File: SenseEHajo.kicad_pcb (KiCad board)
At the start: 2 copper layers, 141 x 56.9 mm, 75 parts, among them IC1 AP3012, IC2 MCP3221, IC3 SN74AUP1G08-Q1, J1 Conn_01x02_Male, J2 REED, J3 RTC ( DS3231), J4 Heizung, J5 Pumpe, J6 Conn_01x05, J7 L, J8 N, J9 Prog, Q1 BSS138, SW1 Reset, SW2 SW1 ( Boot ), SW3 SW2, SW4 SW3, T1 QJ8025, T2 QJ8025, U1 ESP32-WROOM-32, U2 MCP6001-OT, U3 MOC3043M, U4 MOC3043M, U5 TCA9544A, U6 LM1117-3.3

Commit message: CleanUp
Small Cleanup on the PCB
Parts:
- added C18: 10uF, Capacitor_SMD:C_0805_2012Metric_Pad1.15x1.40mm_HandSolder, F.Cu at (154.1, 25.0)
- added C19: 100nF, Capacitor_SMD:C_0805_2012Metric_Pad1.15x1.40mm_HandSolder, F.Cu at (154.1, 26.9)
- moved C4 2.55 mm to (152.7, 28.9), turned to 180 degrees
- moved J6 0.05 mm to (133.2, 68.6)
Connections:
- J3 pad 4: (no net) -> Net-(J3-Pad4)
- LED3 pad 1: (no net) -> Net-(LED3-Pad1)
- U1 pad 10: (no net) -> IO25
- U1 pad 13: (no net) -> IO14
- U1 pad 14: (no net) -> IO12
- U1 pad 16: (no net) -> IO13
- U1 pad 17: (no net) -> Net-(U1-Pad17)
- U1 pad 18: (no net) -> Net-(U1-Pad18)
- U1 pad 19: (no net) -> Net-(U1-Pad19)
- U1 pad 20: (no net) -> Net-(U1-Pad20)
- U1 pad 21: (no net) -> Net-(U1-Pad21)
- U1 pad 22: (no net) -> Net-(U1-Pad22)
- U1 pad 23: (no net) -> IO15
- U1 pad 24: (no net) -> IO2
- U1 pad 30: (no net) -> IO18
- U1 pad 31: (no net) -> IO19
- U1 pad 32: (no net) -> Net-(U1-Pad32)
- U1 pad 37: (no net) -> IO23
- U1 pad 4: (no net) -> SVP
- U1 pad 5: (no net) -> SVN
- U1 pad 6: (no net) -> IO34
- U1 pad 7: (no net) -> IO35
- U3 pad 3: (no net) -> Net-(U3-Pad3)
- U3 pad 5: (no net) -> Net-(U3-Pad5)
- U4 pad 3: (no net) -> Net-(U4-Pad3)
- U4 pad 5: (no net) -> Net-(U4-Pad5)
- U5 pad 11: (no net) -> Net-(U5-Pad11)
- U5 pad 14: (no net) -> Net-(U5-Pad14)
- U5 pad 15: (no net) -> Net-(U5-Pad15)
- U5 pad 16: (no net) -> Net-(U5-Pad16)
- U5 pad 4: (no net) -> Net-(U5-Pad4)
- U5 pad 7: (no net) -> Net-(U5-Pad7)
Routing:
- net GND: track 291.9 -> 283.4 mm, vias 2 -> 78
- net Net-(C1-Pad1): track 49.3 -> 53.8 mm
- net +3V3: track 260.5 -> 264.0 mm
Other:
- board text added: "3V3"
- board text added: "5V"
- board text added: "GND"
- board text added: "Heater"
- board text added: "MCU_RX"
- board text added: "MCU_TX"
- board text added: "Pump"
- board text added: "Schematic + Routing by CalM"
- board text removed: "ACDC1"
- board text removed: "C6"
- board text removed: "C7"
- board text removed: "LED2"
- board text removed: "LED3"
- board text removed: "Schematic and Routing by CalM"

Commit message: Added Netfrequency Detection
This will detect the Netfrequency on IO25 of the ESP32. This is usefull to determine the amount of water pumped to the cup
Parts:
- added IC4: K814P, Package_DIP:DIP-4_W7.62mm, F.Cu at (44.1, 66.0)
- added R5: 10k, Resistor_SMD:R_0805_2012Metric_Pad1.15x1.40mm_HandSolder, F.Cu at (76.1, 64.5)
- added R6: 100k, Resistor_THT:R_Axial_DIN0207_L6.3mm_D2.5mm_P7.62mm_Horizontal, F.Cu at (33.5, 63.0)
- added R7: 100k, Resistor_THT:R_Axial_DIN0207_L6.3mm_D2.5mm_P7.62mm_Horizontal, F.Cu at (24.9, 54.8)
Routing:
- net IO25: track 0.00 -> 140.0 mm, vias 0 -> 7
- net N_230V: track 20.8 -> 48.8 mm
- net L_230V: track 141.2 -> 159.4 mm
- net GND: track 283.4 -> 290.6 mm
- net Net-(IC4-Pad2): track 0.00 -> 5.70 mm
- net +3V3: track 264.0 -> 268.8 mm
- net Net-(R6-Pad1): track 0.00 -> 4.33 mm
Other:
- outline, holes or cut-outs redrawn

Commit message: Small modifications
The AC/DC supply is operating on the edge of it's limits now
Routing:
- net GND: track 290.6 -> 264.2 mm
- net +5V: track 317.7 -> 313.3 mm, vias 5 -> 7
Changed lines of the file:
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@@
     (thickness 1.6)
     (drawings 592)
-    (tracks 1166)
+    (tracks 1169)
     (zones 0)
     (modules 81)
@@
   (segment (start 122.27921 61.74379) (end 119.32682 61.74379) (width 0.25) (layer F.Cu) (net 2))
   (segment (start 124.587 59.436) (end 122.27921 61.74379) (width 0.25) (layer F.Cu) (net 2))
-  (segment (start 60.724644 48.744869) (end 72.413131 48.744869) (width 0.25) (layer F.Cu) (net 2))
-  (segment (start 59.574645 47.59487) (end 60.724644 48.744869) (width 0.25) (layer F.Cu) (net 2))
-  (segment (start 72.413131 48.744869) (end 74.60679 46.55121) (width 0.25) (layer F.Cu) (net 2))
   (segment (start 105.5116 46.8884) (end 105.156 47.244) (width 0.25) (layer F.Cu) (net 2))
   (segment (start 108.368731 52.750429) (end 103.550429 52.750429) (width 0.25) (layer F.Cu) (net 2))
@@
   (segment (start 95.5294 46.988402) (end 95.504 45.4914) (width 0.25) (layer F.Cu) (net 2))
   (segment (start 95.504 45.4914) (end 95.5294 44.9592) (width 0.25) (layer F.Cu) (net 2))
-  (segment (start 83.09039 46.55121) (end 84.1502 45.4914) (width 0.25) (layer F.Cu) (net 2))
-  (segment (start 83.09039 46.55121) (end 74.60679 46.55121) (width 0.25) (layer F.Cu) (net 2))
   (segment (start 140.875001 67.404999) (end 142.533001 65.746999) (width 0.25) (layer B.Cu) (net 2))
   (segment (start 139.528801 67.404999) (end 140.875001 67.404999) (width 0.25) (layer B.Cu) (net 2))
@@
   (via (at 144.0434 42.9006) (size 0.8) (drill 0.4) (layers F.Cu B.Cu) (net 2))
   (via (at 143.7894 39.0906) (size 0.8) (drill 0.4) (layers F.Cu B.Cu) (net 2))
-  (via (at 143.8656 35.687) (size 0.8) (drill 0.4) (layers F.Cu B.Cu) (net 2))
+  (via (at 143.8656 35.9664) (size 0.8) (drill 0.4) (layers F.Cu B.Cu) (net 2))
   (segment (start 148.971 38.989) (end 148.971 38.989) (width 1) (layer F.Cu) (net 2))
   (via (at 148.971 38.989) (size 0.8) (drill 0.4) (layers F.Cu B.Cu) (net 2))
@@
   (segment (start 73.047862 69.25599) (end 73.61901 69.827138) (width 1.5) (layer B.Cu) (net 8))
   (segment (start 70.62759 69.25599) (end 73.047862 69.25599) (width 1.5) (layer B.Cu) (net 8))
-  (segment (start 131.4238 68.58) (end 130.485799 69.518001) (width 1) (layer B.Cu) (net 8))
   (segment (start 133.2738 68.58) (end 131.4238 68.58) (width 1) (layer B.Cu) (net 8))
-  (segment (start 125.857 65.5066) (end 125.857 59.436) (width 1) (layer B.Cu) (net 8))
   (via (at 113.1062 56.4896) (size 0.8) (drill 0.4) (layers F.Cu B.Cu) (net 8))
   (segment (start 113.1062 54.0692) (end 114.808 52.3674) (width 1) (layer F.Cu) (net 8))
@@
   (segment (start 119.509402 45.087402) (end 108.1532 45.0596) (width 1) (layer B.Cu) (net 8))
   (segment (start 128.982999 69.518001) (end 128.238999 69.518001) (width 1) (layer B.Cu) (net 8))
-  (segment (start 130.485799 69.518001) (end 128.982999 69.518001) (width 1) (layer B.Cu) (net 8))
   (segment (start 114.200199 69.518001) (end 113.6142 70.104) (width 1) (layer B.Cu) (net 8))
   (segment (start 113.6142 70.104) (end 113.6142 75.9206) (width 1) (layer B.Cu) (net 8))
-  (segment (start 125.8824 60.168506) (end 125.8824 69.5706) (width 1) (layer B.Cu) (net 8))
-  (segment (start 125.857 60.143106) (end 125.8824 60.168506) (width 1) (layer B.Cu) (net 8))
-  (segment (start 128.982999 69.518001) (end 125.8824 69.5706) (width 1) (layer B.Cu) (net 8))
-  (segment (start 125.857 59.436) (end 125.857 60.143106) (width 1) (layer B.Cu) (net 8))
-  (segment (start 125.8824 69.5706) (end 114.200199 69.518001) (width 1) (layer B.Cu) (net 8))
+  (segment (start 125.8824 60.117706) (end 125.8824 69.5198) (width 1) (layer B.Cu) (net 8))
   (segment (start 124.333 35.151198) (end 124.3584 35.125798) (width 1) (layer B.Cu) (net 8))
   (segment (start 124.333 36.703) (end 124.333 35.151198) (width 1) (layer B.Cu) (net 8))
@@
   (segment (start 104.14 69.215) (end 104.14 71.0184) (width 0.25) (layer B.Cu) (net 8))
   (segment (start 103.8606 68.9356) (end 104.14 69.215) (width 0.25) (layer B.Cu) (net 8))
-  (segment (start 61.5442 58.220894) (end 74.705494 45.0596) (width 1) (layer B.Cu) (net 8))
+  (segment (start 61.5442 58.220894) (end 65.165747 54.599347) (width 1) (layer B.Cu) (net 8))
   (segment (start 61.5442 58.928) (end 61.5442 58.220894) (width 1) (layer B.Cu) (net 8))
   (segment (start 108.1532 45.0596) (end 77.6478 45.0596) (width 1) (layer B.Cu) (net 8))
   (segment (start 74.705494 45.0596) (end 77.6478 45.0596) (width 1) (layer B.Cu) (net 8))
+  (via (at 65.165747 54.599347) (size 0.8) (drill 0.4) (layers F.Cu B.Cu) (net 8))
+  (segment (start 72.836547 46.928547) (end 74.705494 45.0596) (width 1) (layer B.Cu) (net 8))
+  (via (at 72.836547 46.928547) (size 0.8) (drill 0.4) (layers F.Cu B.Cu) (net 8))
+  (segment (start 65.565746 54.199348) (end 72.836547 46.928547) (width 1) (layer F.Cu) (net 8))
+  (segment (start 65.165747 54.599347) (end 65.565746 54.199348) (width 1) (layer F.Cu) (net 8))
+  (segment (start 114.200199 69.518001) (end 123.467601 69.518001) (width 1) (layer B.Cu) (net 8))
+  (segment (start 130.485799 69.518001) (end 130.556 69.5198) (width 1) (layer B.Cu) (net 8))
+  (segment (start 123.4694 69.5198) (end 130.556 69.5198) (width 1) (layer B.Cu) (net 8))
+  (segment (start 123.467601 69.518001) (end 123.4694 69.5198) (width 1) (layer B.Cu) (net 8))
+  (segment (start 130.556 69.5198) (end 128.982999 69.518001) (width 1) (layer B.Cu) (net 8))
+  (segment (start 130.556 69.4478) (end 131.4238 68.58) (width 1) (layer B.Cu) (net 8))
+  (segment (start 130.556 69.5198) (end 130.556 69.4478) (width 1) (layer B.Cu) (net 8))
+  (segment (start 125.8824 59.5122) (end 125.8824 60.117706) (width 1) (layer B.Cu) (net 8))
+  (segment (start 125.857 59.4868) (end 125.8824 59.5122) (width 1) (layer B.Cu) (net 8))
+  (segment (start 125.857 59.436) (end 125.857 59.4868) (width 1) (layer B.Cu) (net 8))
   (segment (start 113.6122 70.4142) (end 113.4798 70.2818) (width 1) (layer F.Cu) (net 9))
   (segment (start 113.6122 72.4916) (end 113.6122 70.4142) (width 1) (layer F.Cu) (net 9))

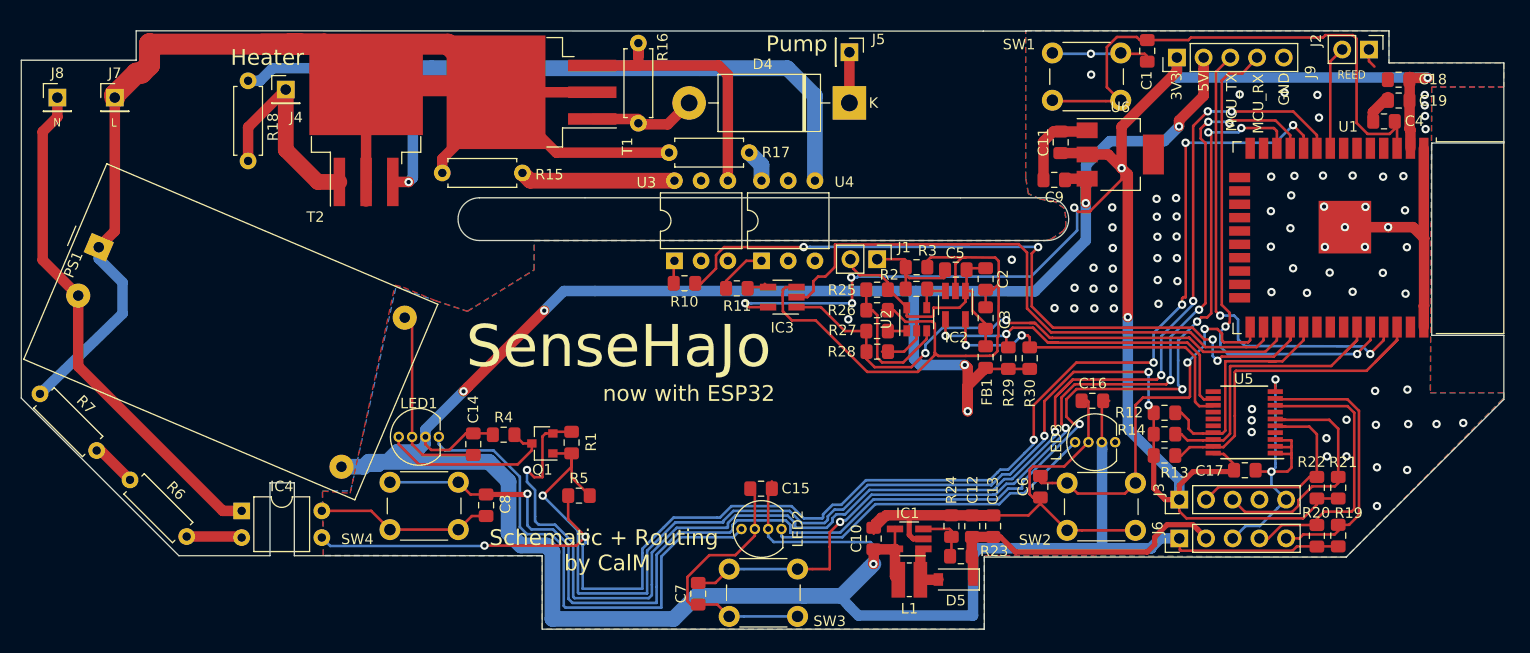
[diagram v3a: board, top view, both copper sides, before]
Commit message: Version3
Ordered Proto for Version 3
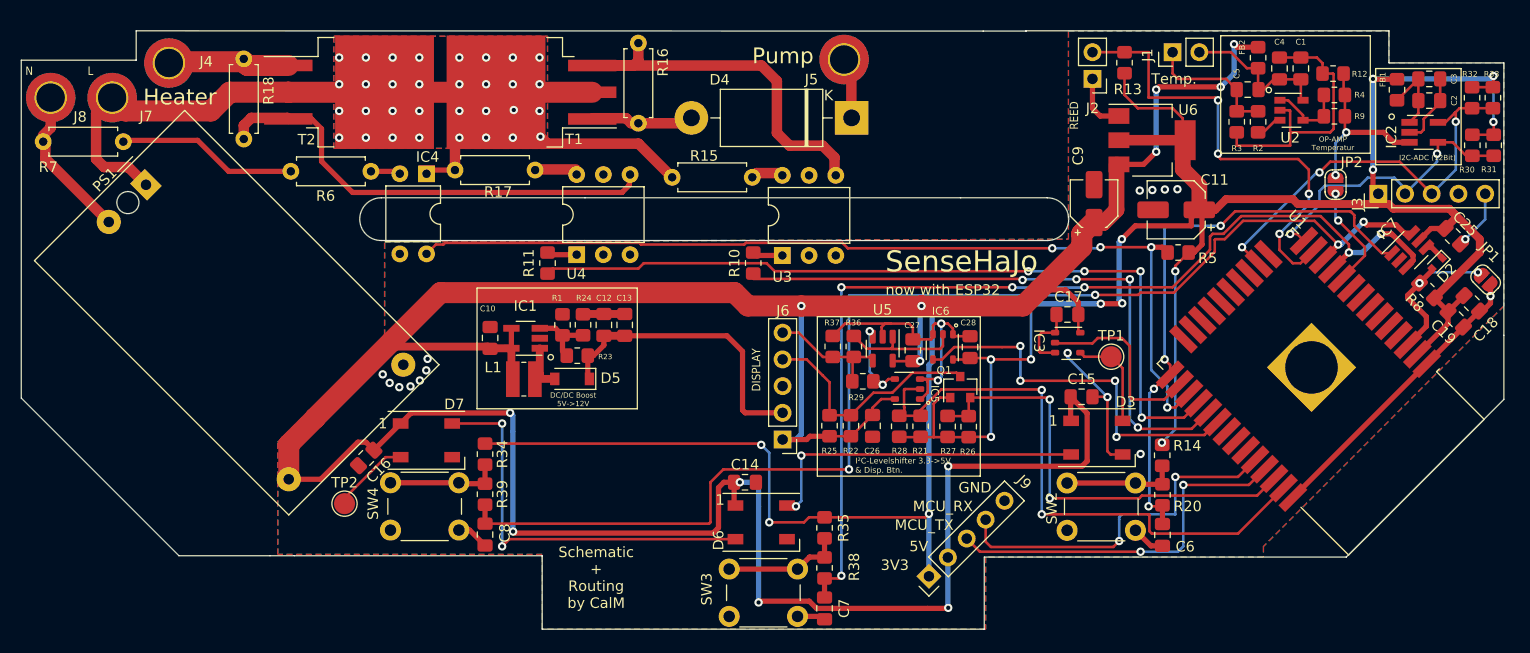
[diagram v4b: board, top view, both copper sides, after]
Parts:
- removed LED1, LED2, LED3: WS2812D, WS2812D:WS2812D_THT
- removed R19: 15k, Resistor_SMD:R_0805_2012Metric_Pad1.15x1.40mm_HandSolder
- removed SW1: Reset, Button_Switch_THT:SW_PUSH_6mm
- added C25: 100nF / 10V, Capacitor_SMD:C_0805_2012Metric_Pad1.18x1.45mm_HandSolder, F.Cu at (159.2, 39.8)
- added C26: 100nF / 10V, Capacitor_SMD:C_0805_2012Metric_Pad1.18x1.45mm_HandSolder, F.Cu at (104.1, 57.9)
- added C27: 100nF / 10V, Capacitor_SMD:C_0805_2012Metric_Pad1.18x1.45mm_HandSolder, F.Cu at (107.9, 50.7)
- added C28: 100nF / 10V, Capacitor_SMD:C_0805_2012Metric_Pad1.18x1.45mm_HandSolder, F.Cu at (113.3, 50.4)
- added D2: D_Schottky, Diode_SMD:D_SOD-523, F.Cu at (157.7, 42.4)
- added D3: WS2812B, LED_SMD:LED_WS2812B_PLCC4_5.0x5.0mm_P3.2mm, F.Cu at (125.4, 59.0)
- added D6: WS2812B, LED_SMD:LED_WS2812B_PLCC4_5.0x5.0mm_P3.2mm, F.Cu at (93.5, 67.1)
- added D7: WS2812B, LED_SMD:LED_WS2812B_PLCC4_5.0x5.0mm_P3.2mm, F.Cu at (61.6, 59.3)
- added FB2: Ferrite_Bead, Resistor_SMD:R_0805_2012Metric_Pad1.20x1.40mm_HandSolder, F.Cu at (140.7, 22.9)
- added IC5: 74LVC1G125, SC-74A_SOT753:SC-74A, F.Cu at (108.6, 55.3)
- added IC6: 74LVC1G125, SC-74A_SOT753:SC-74A, F.Cu at (111.7, 49.2)
- added IC7: 74LVC1G10, Package_TO_SOT_SMD:SOT-23-6_Handsoldering, F.Cu at (155.1, 41.2)
- added JP1: Jumper_2_Open, Jumper:SolderJumper-2_P1.3mm_Open_RoundedPad1.0x1.5mm, F.Cu at (162.4, 44.0)
- added JP2: Jumper_2_Open, Jumper:SolderJumper-2_P1.3mm_Open_RoundedPad1.0x1.5mm, F.Cu at (148.1, 34.9)
- added R31: 10k, Resistor_SMD:R_0805_2012Metric_Pad1.20x1.40mm_HandSolder, F.Cu at (163.1, 31.2)
- added R32: 10k, Resistor_SMD:R_0805_2012Metric_Pad1.20x1.40mm_HandSolder, F.Cu at (161.1, 26.7)
- added R33: 10k, Resistor_SMD:R_0805_2012Metric_Pad1.20x1.40mm_HandSolder, F.Cu at (163.0, 26.7)
- added R34: 10k, Resistor_SMD:R_0805_2012Metric_Pad1.20x1.40mm_HandSolder, F.Cu at (67.2, 60.6)
- added R35: 10k, Resistor_SMD:R_0805_2012Metric_Pad1.20x1.40mm_HandSolder, F.Cu at (99.5, 67.6)
- added R36: 10k, Resistor_SMD:R_0805_2012Metric_Pad1.20x1.40mm_HandSolder, F.Cu at (102.3, 50.3)
- added R37: 1k, Resistor_SMD:R_0805_2012Metric_Pad1.20x1.40mm_HandSolder, F.Cu at (100.3, 50.3)
- added R38: 1k, Resistor_SMD:R_0805_2012Metric_Pad1.20x1.40mm_HandSolder, F.Cu at (99.5, 71.4)
- added R39: 1k, Resistor_SMD:R_0805_2012Metric_Pad1.20x1.40mm_HandSolder, F.Cu at (67.2, 64.4)
- added R8: 10k, Resistor_SMD:R_0805_2012Metric_Pad1.20x1.40mm_HandSolder, F.Cu at (156.8, 45.0)
- added R9: 10k, Resistor_SMD:R_0805_2012Metric_Pad1.20x1.40mm_HandSolder, F.Cu at (148.0, 28.4)
- added REF**: MountingHole_2.1mm, MountingHole:MountingHole_2.1mm, F.Cu at (33.2, 36.7)
- added TP1: TestPoint, TestPoint:TestPoint_Pad_D2.0mm, F.Cu at (126.7, 51.3)
- added TP2: TestPoint, TestPoint:TestPoint_Pad_D2.0mm, F.Cu at (53.8, 65.3)
- C1: value 100nF / 25V -> 1uF / 10V; footprint Capacitor_SMD:C_0805_2012Metric_Pad1.15x1.40mm_HandSolder -> Capacitor_SMD:C_0805_2012Metric_Pad1.18x1.45mm_HandSolder
- C10, C12, C13, C3: footprint Capacitor_SMD:C_0805_2012Metric_Pad1.15x1.40mm_HandSolder -> Capacitor_SMD:C_0805_2012Metric_Pad1.18x1.45mm_HandSolder
- C11: value 100uF -> 47uF/10V; footprint Capacitor_SMD:C_0805_2012Metric_Pad1.15x1.40mm_HandSolder -> Capacitor_SMD:CP_Elec_5x5.3
- C14, C15, C16, C17, C19, C5, C7, C8: value 100nF -> 100nF / 10V; footprint Capacitor_SMD:C_0805_2012Metric_Pad1.15x1.40mm_HandSolder -> Capacitor_SMD:C_0805_2012Metric_Pad1.18x1.45mm_HandSolder
- C18: value 10uF -> 10uF / 10V; footprint Capacitor_SMD:C_0805_2012Metric_Pad1.15x1.40mm_HandSolder -> Capacitor_SMD:C_0805_2012Metric_Pad1.18x1.45mm_HandSolder
- C2: value 100nf / 10V -> 100nF / 10V; footprint Capacitor_SMD:C_0805_2012Metric_Pad1.15x1.40mm_HandSolder -> Capacitor_SMD:C_0805_2012Metric_Pad1.18x1.45mm_HandSolder
- C4: value 10uF / 25V -> 100nF / 10V; footprint Capacitor_SMD:C_0805_2012Metric_Pad1.15x1.40mm_HandSolder -> Capacitor_SMD:C_0805_2012Metric_Pad1.18x1.45mm_HandSolder
- C6: value 100nF / 25V -> 100nF / 10V; footprint Capacitor_SMD:C_0805_2012Metric_Pad1.15x1.40mm_HandSolder -> Capacitor_SMD:C_0805_2012Metric_Pad1.18x1.45mm_HandSolder
- C9: value 10uF -> 10uF/10V; footprint Capacitor_SMD:C_0805_2012Metric_Pad1.15x1.40mm_HandSolder -> Capacitor_SMD:CP_Elec_4x4.5
- FB1: footprint Capacitor_SMD:C_0805_2012Metric_Pad1.15x1.40mm_HandSolder -> Resistor_SMD:R_0805_2012Metric_Pad1.20x1.40mm_HandSolder
- IC3: value SN74AUP1G08-Q1 -> 74LVC1G125; footprint Package_TO_SOT_SMD:SOT-23-5_HandSoldering -> SC-74A_SOT753:SC-74A
- J4: value Heizung -> Heizung L; footprint Connector_PinHeader_2.54mm:PinHeader_1x01_P2.54mm_Vertical -> MountingHole:MountingHole_2.7mm_M2.5_DIN965_Pad_TopBottom
- J5: value Pumpe -> Pumpe L; footprint Connector_PinHeader_2.54mm:PinHeader_1x01_P2.54mm_Vertical -> MountingHole:MountingHole_2.7mm_M2.5_DIN965_Pad_TopBottom
- J7, J8: footprint Connector_PinHeader_2.54mm:PinHeader_1x01_P2.54mm_Vertical -> MountingHole:MountingHole_2.7mm_M2.5_DIN965_Pad_TopBottom
- R1, R10, R11, R2, R3, R5: footprint Resistor_SMD:R_0805_2012Metric_Pad1.15x1.40mm_HandSolder -> Resistor_SMD:R_0805_2012Metric_Pad1.20x1.40mm_HandSolder
- R12, R24: value 4k7 -> 10k; footprint Resistor_SMD:R_0805_2012Metric_Pad1.15x1.40mm_HandSolder -> Resistor_SMD:R_0805_2012Metric_Pad1.20x1.40mm_HandSolder
- R13, R14, R21, R22, R30: value 2k2 -> 10k; footprint Resistor_SMD:R_0805_2012Metric_Pad1.15x1.40mm_HandSolder -> Resistor_SMD:R_0805_2012Metric_Pad1.20x1.40mm_HandSolder
- R20: value 15k -> 1k; footprint Resistor_SMD:R_0805_2012Metric_Pad1.15x1.40mm_HandSolder -> Resistor_SMD:R_0805_2012Metric_Pad1.20x1.40mm_HandSolder
- R23: value 39k -> 43.2k; footprint Resistor_SMD:R_0805_2012Metric_Pad1.15x1.40mm_HandSolder -> Resistor_SMD:R_0805_2012Metric_Pad1.20x1.40mm_HandSolder
- R25: value 1k -> 10k; footprint Resistor_SMD:R_0805_2012Metric_Pad1.15x1.40mm_HandSolder -> Resistor_SMD:R_0805_2012Metric_Pad1.20x1.40mm_HandSolder
- R26: value 3k9 -> 10k; footprint Resistor_SMD:R_0805_2012Metric_Pad1.15x1.40mm_HandSolder -> Resistor_SMD:R_0805_2012Metric_Pad1.20x1.40mm_HandSolder
- R27: value 1k8 -> 10k; footprint Resistor_SMD:R_0805_2012Metric_Pad1.15x1.40mm_HandSolder -> Resistor_SMD:R_0805_2012Metric_Pad1.20x1.40mm_HandSolder
- R28: value 3k3 -> 10k; footprint Resistor_SMD:R_0805_2012Metric_Pad1.15x1.40mm_HandSolder -> Resistor_SMD:R_0805_2012Metric_Pad1.20x1.40mm_HandSolder
- R29: value 2k2 -> 100R; footprint Resistor_SMD:R_0805_2012Metric_Pad1.15x1.40mm_HandSolder -> Resistor_SMD:R_0805_2012Metric_Pad1.20x1.40mm_HandSolder
- R4: value 10k -> 10k (DNP); footprint Resistor_SMD:R_0805_2012Metric_Pad1.15x1.40mm_HandSolder -> Resistor_SMD:R_0805_2012Metric_Pad1.20x1.40mm_HandSolder
- SW3: value SW2 -> MACHINE_SW2
- SW4: value SW3 -> MACHINE_SW3
- U1: footprint RF_Module:ESP32-WROOM-32 -> ESP32_Handsolder:ESP32-WROOM-32_HandSolder
- U5: value TCA9544A -> MCP6001-OT; footprint Package_SO:TSSOP-20_4.4x6.5mm_P0.65mm -> Package_TO_SOT_SMD:SOT-23-5
- U6: footprint Package_TO_SOT_SMD:SOT-223 -> Package_TO_SOT_SMD:SOT-223-3_TabPin2
- moved R4 85.3 mm to (148.0, 26.4), turned to 180 degrees
- moved C16 69.3 mm to (55.9, 60.9), turned to -135 degrees
- moved R5 61.5 mm to (133.1, 41.4)
- moved J9 54.7 mm to (109.4, 72.2), turned to 135 degrees
- moved C3 47.9 mm to (157.0, 24.9), turned to 0 degrees
- moved IC2 47.5 mm to (156.5, 30.0), turned to 0 degrees
- moved R30 46.7 mm to (161.1, 31.2)
- moved FB1 46.6 mm to (153.9, 25.9), turned to -90 degrees
- moved C2 45.5 mm to (157.0, 27.0), turned to 0 degrees
- moved R22 44.7 mm to (102.0, 57.9), turned to -90 degrees
- moved L1 41.3 mm to (70.9, 53.4)
- moved C10 41.2 mm to (67.7, 49.5)
- moved D5 41.2 mm to (75.5, 53.4)
- moved R23 41.2 mm to (76.0, 51.2)
- moved IC1 41.2 mm to (71.1, 49.6)
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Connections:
- C17 pad 2: +3V3 -> +5V
- C5 pad 1: Net-(C2-Pad1) -> Net-(C1-Pad1)
- C6 pad 2: Net-(C6-Pad2) -> SW1
- C7 pad 2: Net-(C7-Pad2) -> SW2
- C8 pad 2: Net-(C8-Pad2) -> SW3
- FB1 pad 1: +5V -> +3V3
- IC2 pad 4: SDA_ADC -> SDA_3V3
- IC2 pad 5: SCL_ADC -> SCL_3V3
- IC3 pad 1: ~OVERTEMP -> GND
- IC3 pad 2: Heizung -> WS2812_3V3
- IC3 pad 4: Net-(IC3-Pad4) -> Net-(D3-Pad4)
- IC3 pad 5: +3V3 -> +5V
- IC4 pad 1: N_230V -> L_230V
- IC4 pad 3: IO25 -> GND
- IC4 pad 4: GND -> MAINS_HALVEWAVES
- J1 pad 2: Net-(C2-Pad1) -> Net-(C1-Pad1)
- J2 pad 2: REED -> REED_IN
- J3 pad 2: SDA_RTC -> SDA_3V3
- J3 pad 3: SCL_RTC -> SCL_3V3
- J3 pad 4: Net-(J3-Pad4) -> unconnected-(J3-Pad4)
- Q1 pad 2: WS2812_3V3 -> I2C_DSP_SDA
- Q1 pad 3: Net-(LED1-Pad4) -> SDA_DSP
- R1 pad 1: +3V3 -> Net-(IC1-Pad3)
- R1 pad 2: WS2812_3V3 -> GND
- R10 pad 2: Pumpe -> PUMP_MOC
- R11 pad 2: Net-(IC3-Pad4) -> Heizung_MOC
- R12 pad 1: +3V3 -> Net-(IC2-Pad3)
- R12 pad 2: I2C_INT -> GND
- R13 pad 2: I2C_SCL -> REED_IN
- R14 pad 2: I2C_SDA -> Net-(R14-Pad2)
- R2 pad 2: Net-(IC2-Pad3) -> Net-(R2-Pad2)
- R20 pad 1: +5V -> Net-(R14-Pad2)
- R20 pad 2: SDA_DSP -> SW1
- R21 pad 1: +3V3 -> I2C_DSP_SCL
- R21 pad 2: SCL_RTC -> +3V3
- R22 pad 1: +3V3 -> SDA_DSP
- R22 pad 2: SDA_RTC -> +5V
- R25 pad 1: Net-(C2-Pad1) -> +5V
- R25 pad 2: Net-(R25-Pad2) -> SDA_DSP
- R26 pad 1: Net-(R25-Pad2) -> I2C_DSP_SDA
- R26 pad 2: GND -> +3V3
- R27 pad 1: ~OVERTEMP -> +3V3
- R27 pad 2: Net-(R27-Pad2) -> I2C_DSP_SDA
- R28 pad 1: ~OVERTEMP -> +3V3
- R28 pad 2: GND -> I2C_DSP_SCL
- R29 pad 1: +5V -> SCL_DSP
- R29 pad 2: SDA_ADC -> Net-(IC5-Pad4)
- R30 pad 1: +5V -> SDA_3V3
- R30 pad 2: SCL_ADC -> +3V3
- R4 pad 1: +5V -> Net-(IC2-Pad3)
- R4 pad 2: Net-(LED1-Pad4) -> Net-(R4-Pad2)
- R5 pad 1: IO25 -> MAINS_HALVEWAVES
- R7 pad 1: L_230V -> N_230V
- SW2 pad 1: Net-(C6-Pad2) -> Net-(R14-Pad2)
- SW3 pad 1: Net-(C7-Pad2) -> Net-(R35-Pad2)
- SW4 pad 1: Net-(C8-Pad2) -> Net-(R34-Pad2)
- U1 pad 10: IO25 -> ESP32_ADC
- U1 pad 11: Net-(C7-Pad2) -> SW2
- U1 pad 12: Net-(C8-Pad2) -> SW3
- U1 pad 13: IO14 -> REED_IN
- U1 pad 14: IO12 -> SDA_3V3
- U1 pad 16: IO13 -> SCL_3V3
- U1 pad 17: Net-(U1-Pad17) -> unconnected-(U1-Pad17)
- U1 pad 18: Net-(U1-Pad18) -> unconnected-(U1-Pad18)
- U1 pad 19: Net-(U1-Pad19) -> unconnected-(U1-Pad19)
- U1 pad 20: Net-(U1-Pad20) -> unconnected-(U1-Pad20)
- U1 pad 21: Net-(U1-Pad21) -> unconnected-(U1-Pad21)
- U1 pad 22: Net-(U1-Pad22) -> unconnected-(U1-Pad22)
- U1 pad 23: IO15 -> unconnected-(U1-Pad23)
- U1 pad 24: IO2 -> unconnected-(U1-Pad24)
- U1 pad 25: Net-(C6-Pad2) -> SW1
- U1 pad 26: Heizung -> WS2812_3V3
- U1 pad 27: ~OVERTEMP -> MAINS_HALVEWAVES
- U1 pad 28: Pumpe -> Heizung_MOC
- U1 pad 29: I2C_INT -> PUMP_MOC
- U1 pad 3: Net-(C1-Pad1) -> Net-(D2-Pad2)
- U1 pad 30: IO18 -> DISP_BTN
- U1 pad 31: IO19 -> unconnected-(U1-Pad31)
- U1 pad 32: Net-(U1-Pad32) -> unconnected-(U1-Pad32)
- U1 pad 33: I2C_SDA -> unconnected-(U1-Pad33)
- U1 pad 36: I2C_SCL -> I2C_DSP_SDA
- U1 pad 37: IO23 -> I2C_DSP_SCL
- U1 pad 4: SVP -> unconnected-(U1-Pad4)
- U1 pad 5: SVN -> unconnected-(U1-Pad5)
- U1 pad 6: IO34 -> unconnected-(U1-Pad6)
- U1 pad 7: IO35 -> unconnected-(U1-Pad7)
- U1 pad 8: REED -> unconnected-(U1-Pad8)
- U1 pad 9: WS2812_3V3 -> unconnected-(U1-Pad9)
- U2 pad 1: Net-(R27-Pad2) -> Net-(R4-Pad2)
- U2 pad 3: Net-(R25-Pad2) -> Net-(R2-Pad2)
- U2 pad 4: Net-(IC2-Pad3) -> Net-(R4-Pad2)
- U2 pad 5: Net-(C2-Pad1) -> Net-(C1-Pad1)
- U3 pad 3: Net-(U3-Pad3) -> unconnected-(U3-Pad3)
- U3 pad 5: Net-(U3-Pad5) -> unconnected-(U3-Pad5)
- U4 pad 3: Net-(U4-Pad3) -> unconnected-(U4-Pad3)
- U4 pad 5: Net-(U4-Pad5) -> unconnected-(U4-Pad5)
- U5 pad 1: GND -> Net-(IC6-Pad2)
- U5 pad 3: GND -> Net-(IC5-Pad4)
- U5 pad 4: Net-(U5-Pad4) -> SCL_DSP
- U5 pad 5: SDA_RTC -> +5V
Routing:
- net IO25: track 140.0 -> 0.00 mm, vias 7 -> 0
- net Net-(C8-Pad2): track 137.7 -> 0.00 mm, vias 6 -> 0
- net GND: track 264.2 -> 135.1 mm, vias 78 -> 18
- net SW3: track 0.00 -> 118.8 mm, vias 0 -> 4
- net WS2812_3V3: track 136.2 -> 17.9 mm, vias 6 -> 0
- net SW2: track 0.00 -> 96.0 mm, vias 0 -> 6
- net Net-(C7-Pad2): track 94.2 -> 0.00 mm, vias 6 -> 0
- net MAINS_HALVEWAVES: track 0.00 -> 90.0 mm, vias 0 -> 4
- net Heizung_MOC: track 0.00 -> 77.0 mm, vias 0 -> 4
- net L_230V: track 159.4 -> 83.0 mm, vias 0 -> 32
- net Pumpe: track 71.8 -> 0.00 mm, vias 4 -> 0
- net PUMP_MOC: track 0.00 -> 57.6 mm, vias 0 -> 4
- net I2C_DSP_SCL: track 0.00 -> 57.4 mm, vias 0 -> 2
- net Heizung: track 57.1 -> 0.00 mm
- net ~OVERTEMP: track 55.4 -> 0.00 mm, vias 2 -> 0
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- added copper zone on B.Cu, net L_230V
- added copper zone on F.Cu, net L_230V
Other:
- outline, holes or cut-outs redrawn
- net class Default removed
- rule pad_to_mask_clearance: 0.051 -> 0
- board text added: "DC/DC Boost 5V->12V"
- board text added: "I2C-ADC (12Bit)"
- board text added: "I²C-Levelshifter 3.3->5V & Disp. Btn."
- board text added: "OP-AMP Temperatur"
- board text added: "Temp."
